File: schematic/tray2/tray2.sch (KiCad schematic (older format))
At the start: 57 parts, among them J1 AVR-ISP-10, J2 Conn_02x10_Odd_Even, J3 Conn_Coaxial, J4 Conn_Coaxial, J5 Conn_Coaxial, Q1 BF998, Q2 BFP196, Q3 BC847, Q4 BC847, U1 74AC253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

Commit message: Update pcb to fix issue
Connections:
- net at U4.7 (XTAL1/PB6): now also J2.15 (Pin_15); no longer J2.5 (Pin_5)
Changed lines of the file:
@@
 EESchema Schematic File Version 4
-LIBS:tray2-cache
 EELAYER 30 0
 EELAYER END
@@
 	7750 3900 10050 3900
 Wire Wire Line
-	10050 3900 10050 3650
-Wire Wire Line
-	10050 3650 10200 3650
-Wire Wire Line
 	7750 5400 7950 5400
 $Comp
@@
 	1    0    0    -1
 $EndComp
+Wire Wire Line
+	10200 4150 10050 4150
+Wire Wire Line
+	10050 4150 10050 3900
 $EndSCHEMATC

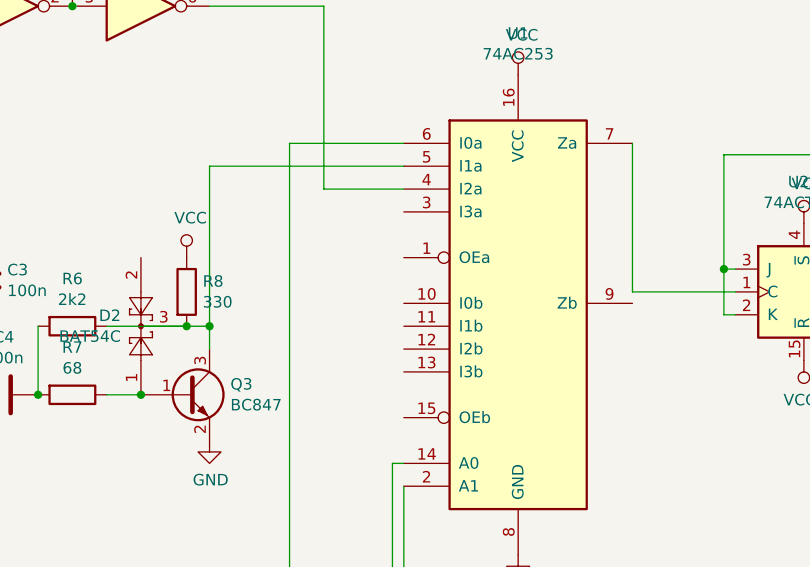
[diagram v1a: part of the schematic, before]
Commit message: Add gnd to oe pin
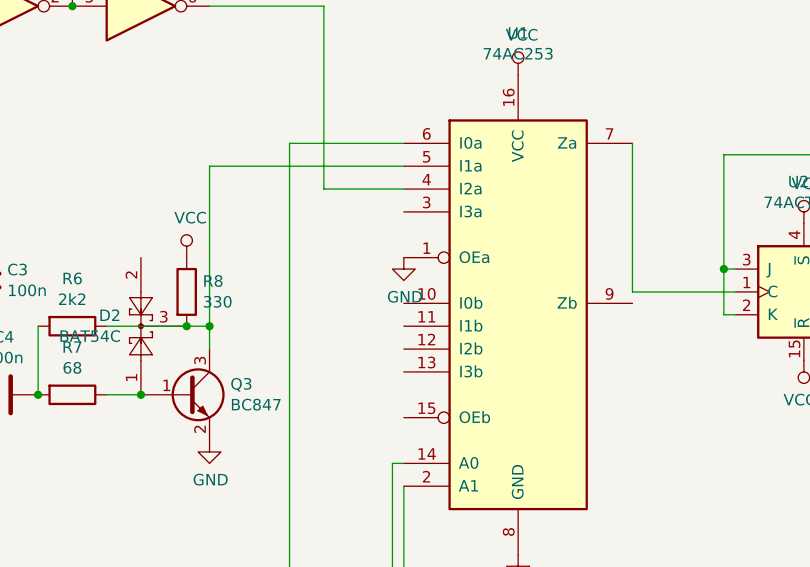
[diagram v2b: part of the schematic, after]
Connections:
- net GND: now also U1.1 (OEa)
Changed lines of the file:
@@
 Wire Wire Line
 	10050 4150 10050 3900
+$Comp
+L power:GND #PWR?
+U 1 1 5E8E86F2
+P 4200 3050
+F 0 "#PWR?" H 4200 2800 50  0001 C CNN
+F 1 "GND" H 4205 2877 50  0000 C CNN
+F 2 "" H 4200 3050 50  0001 C CNN
+F 3 "" H 4200 3050 50  0001 C CNN
+	1    4200 3050
+	1    0    0    -1
+$EndComp
 $EndSCHEMATC

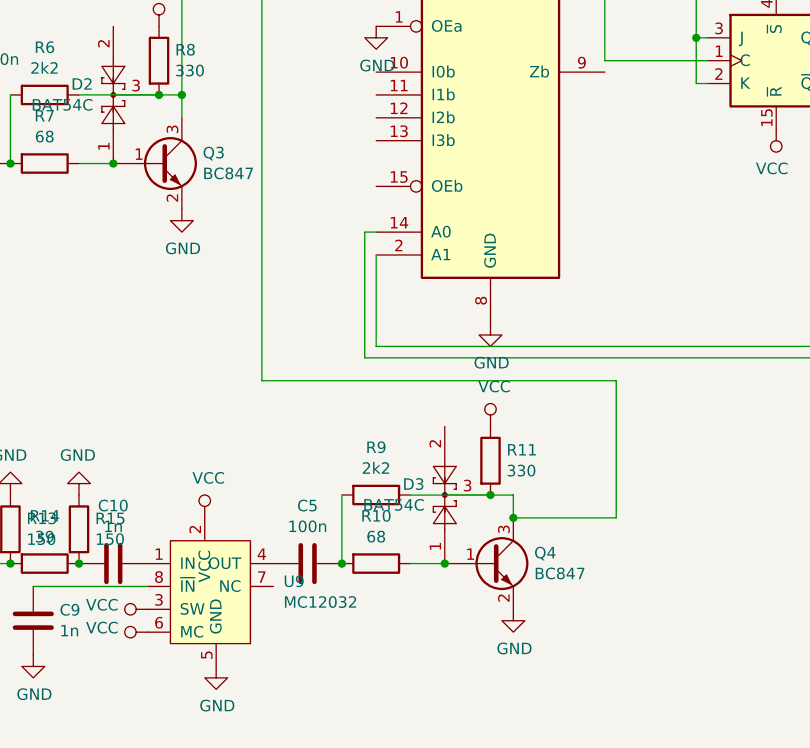
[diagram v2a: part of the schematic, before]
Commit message: Change transistor with bigger fT
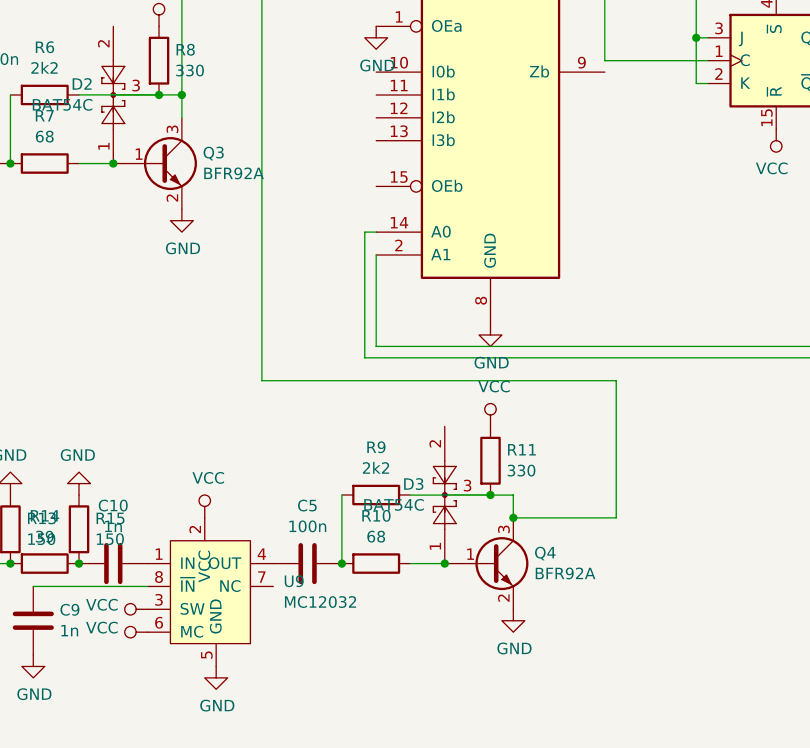
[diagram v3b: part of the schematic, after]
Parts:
- Q3, Q4: value BC847 -> BFR92A
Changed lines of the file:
@@
 P 3250 3650
 F 0 "Q3" H 3441 3696 50  0000 L CNN
-F 1 "BC847" H 3441 3605 50  0000 L CNN
+F 1 "BFR92A" H 3441 3605 50  0000 L CNN
 F 2 "Package_TO_SOT_SMD:SOT-23" H 3450 3575 50  0001 L CIN
 F 3 "http://www.infineon.com/dgdl/Infineon-BC847SERIES_BC848SERIES_BC849SERIES_BC850SERIES-DS-v01_01-en.pdf?fileId=db3a304314dca389011541d4630a1657" H 3250 3650 50  0001 L CNN
@@
 P 4700 5400
 F 0 "Q4" H 4891 5446 50  0000 L CNN
-F 1 "BC847" H 4891 5355 50  0000 L CNN
+F 1 "BFR92A" H 4891 5355 50  0000 L CNN
 F 2 "Package_TO_SOT_SMD:SOT-23" H 4900 5325 50  0001 L CIN
 F 3 "http://www.infineon.com/dgdl/Infineon-BC847SERIES_BC848SERIES_BC849SERIES_BC850SERIES-DS-v01_01-en.pdf?fileId=db3a304314dca389011541d4630a1657" H 4700 5400 50  0001 L CNN
@@
 	10050 4150 10050 3900
 $Comp
-L power:GND #PWR?
+L power:GND #PWR0110
 U 1 1 5E8E86F2
 P 4200 3050
-F 0 "#PWR?" H 4200 2800 50  0001 C CNN
+F 0 "#PWR0110" H 4200 2800 50  0001 C CNN
 F 1 "GND" H 4205 2877 50  0000 C CNN
 F 2 "" H 4200 3050 50  0001 C CNN

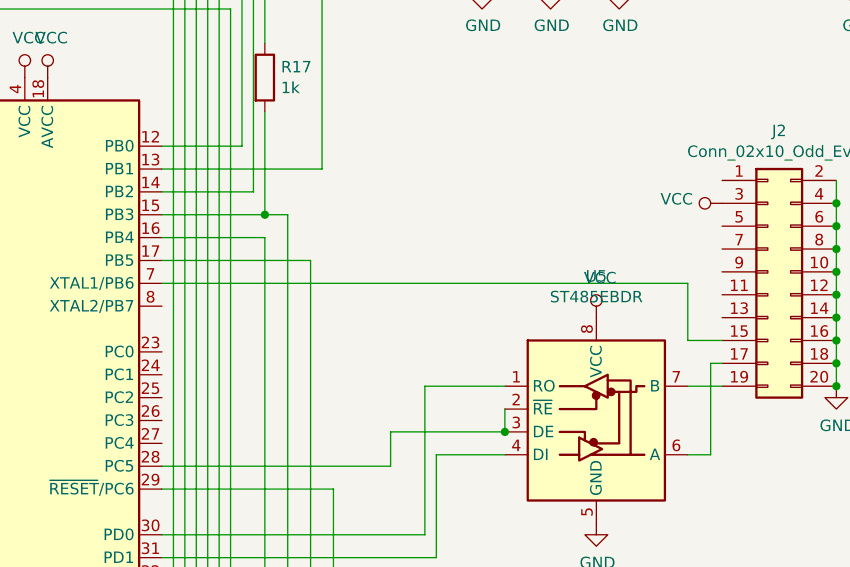
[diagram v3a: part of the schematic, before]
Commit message: Add capacitor on path of clock
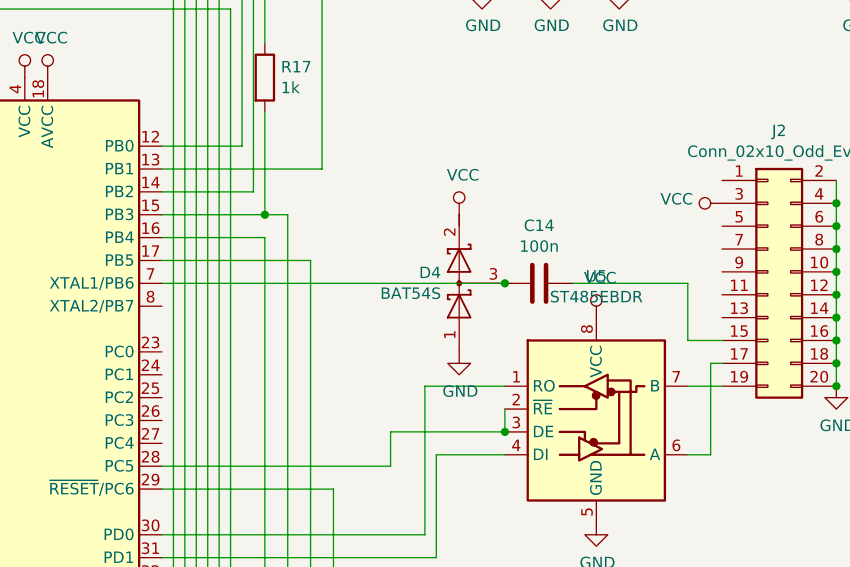
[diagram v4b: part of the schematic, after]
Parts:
- added C14: 100n, Capacitor_SMD:C_0805_2012Metric_Pad1.15x1.40mm_HandSolder, symbol Device:C
- added D4: BAT54S, Package_TO_SOT_SMD:SOT-23, symbol Device:D_Schottky_x2_Serial_AKC
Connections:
- net GND: now also D4.1 (A)
- net VCC: now also D4.2 (K)
- net at U4.7 (XTAL1/PB6): now also C14.2, D4.3 (common); no longer J2.15 (Pin_15)
- new net: C14.1, J2.15 (Pin_15)
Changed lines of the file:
@@
 	8200 3700 7750 3700
 Wire Wire Line
-	7750 3900 10050 3900
+	7750 3900 9250 3900
 Wire Wire Line
 	7750 5400 7950 5400
@@
 	1    0    0    -1
 $EndComp
+$Comp
+L Device:D_Schottky_x2_Serial_AKC D4
+U 1 1 5EA63485
+P 9050 3900
+F 0 "D4" V 9096 3979 50  0000 L CNN
+F 1 "BAT54S" V 9005 3979 50  0000 L CNN
+F 2 "Package_TO_SOT_SMD:SOT-23" H 9050 3900 50  0001 C CNN
+F 3 "~" H 9050 3900 50  0001 C CNN
+	1    9050 3900
+	0    -1   -1   0
+$EndComp
+Connection ~ 9250 3900
+$Comp
+L power:VCC #PWR012
+U 1 1 5EA70293
+P 9050 3600
+F 0 "#PWR012" H 9050 3450 50  0001 C CNN
+F 1 "VCC" H 9067 3773 50  0000 C CNN
+F 2 "" H 9050 3600 50  0001 C CNN
+F 3 "" H 9050 3600 50  0001 C CNN
+	1    9050 3600
+	1    0    0    -1
+$EndComp
+$Comp
+L power:GND #PWR013
+U 1 1 5EA70E70
+P 9050 4200
+F 0 "#PWR013" H 9050 3950 50  0001 C CNN
+F 1 "GND" H 9055 4027 50  0000 C CNN
+F 2 "" H 9050 4200 50  0001 C CNN
+F 3 "" H 9050 4200 50  0001 C CNN
+	1    9050 4200
+	1    0    0    -1
+$EndComp
+$Comp
+L Device:C C14
+U 1 1 5EA720FE
+P 9400 3900
+F 0 "C14" V 9148 3900 50  0000 C CNN
+F 1 "100n" V 9239 3900 50  0000 C CNN
+F 2 "Capacitor_SMD:C_0805_2012Metric_Pad1.15x1.40mm_HandSolder" H 9438 3750 50  0001 C CNN
+F 3 "~" H 9400 3900 50  0001 C CNN
+	1    9400 3900
+	0    1    1    0
+$EndComp
+Wire Wire Line
+	10050 3900 9550 3900
 $EndSCHEMATC

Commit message: Use 100 resistor instead capacitor
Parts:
- R18: renamed from C14; value 100n -> 100; footprint Capacitor_SMD:C_0805_2012Metric_Pad1.15x1.40mm_HandSolder -> Resistor_SMD:R_0805_2012Metric_Pad1.15x1.40mm_HandSolder; symbol Device:C -> Device:R
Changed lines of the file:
@@
 $EndComp
 $Comp
-L Device:C C14
+L Device:R R18
 U 1 1 5EA720FE
 P 9400 3900
-F 0 "C14" V 9148 3900 50  0000 C CNN
-F 1 "100n" V 9239 3900 50  0000 C CNN
-F 2 "Capacitor_SMD:C_0805_2012Metric_Pad1.15x1.40mm_HandSolder" H 9438 3750 50  0001 C CNN
+F 0 "R18" V 9193 3900 50  0000 C CNN
+F 1 "100" V 9284 3900 50  0000 C CNN
+F 2 "Resistor_SMD:R_0805_2012Metric_Pad1.15x1.40mm_HandSolder" H 9438 3750 50  0001 C CNN
 F 3 "~" H 9400 3900 50  0001 C CNN
 	1    9400 3900
